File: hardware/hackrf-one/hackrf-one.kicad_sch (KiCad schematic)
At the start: 0 parts

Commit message: HackRF One: update dates
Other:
- company: Copyright 2012-2020 Great Scott Gadgets -> Copyright 2012-2022 Great Scott Gadgets
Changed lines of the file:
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@@
   (title_block
     (title "HackRF One")
-    (date "2021-09-28")
+    (date "2022-08-28")
     (rev "r9")
-    (company "Copyright 2012-2020 Great Scott Gadgets")
+    (company "Copyright 2012-2022 Great Scott Gadgets")
     (comment 1 "Michael Ossmann")
     (comment 2 "Licensed under the CERN-OHL-P v2")

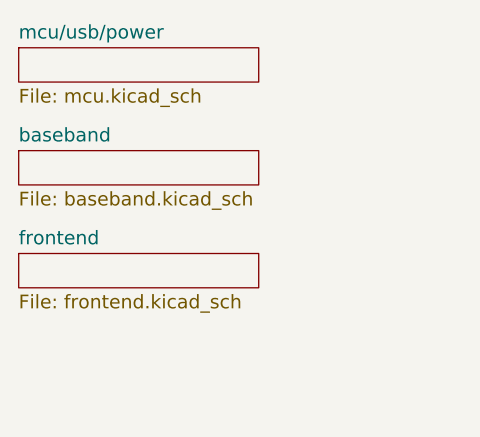
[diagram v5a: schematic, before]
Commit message: HackRF One: change U19 from Si5351C to Si5351A
add clock distribution and detection
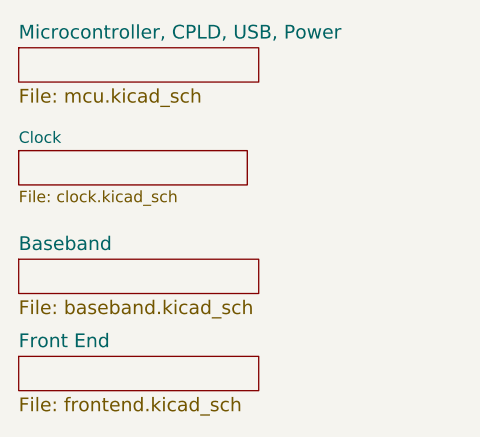
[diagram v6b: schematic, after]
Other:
- sheet baseband renamed Baseband
- sheet frontend renamed Front End
- sheet mcu/usb/power renamed Microcontroller, CPLD, USB, Power
- added sheet Clock (clock.kicad_sch)
